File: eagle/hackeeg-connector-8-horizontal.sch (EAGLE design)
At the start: 21 parts

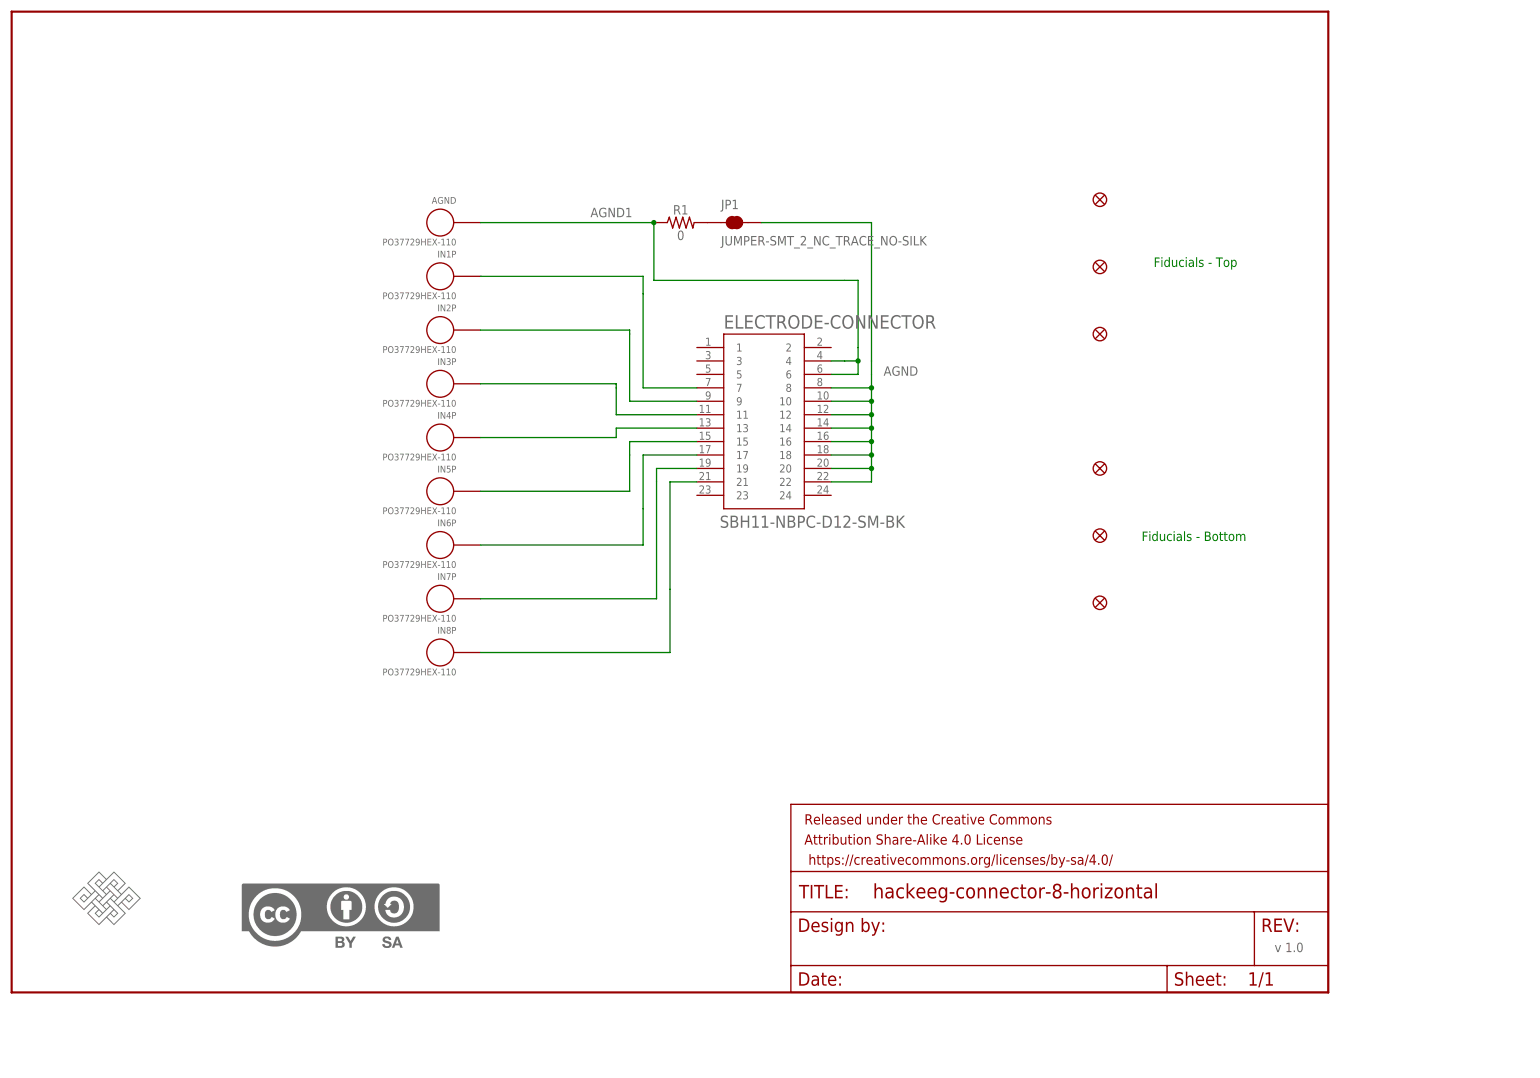
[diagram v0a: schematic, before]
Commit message: relicense to CERN OHL 1.2 - sch and brd
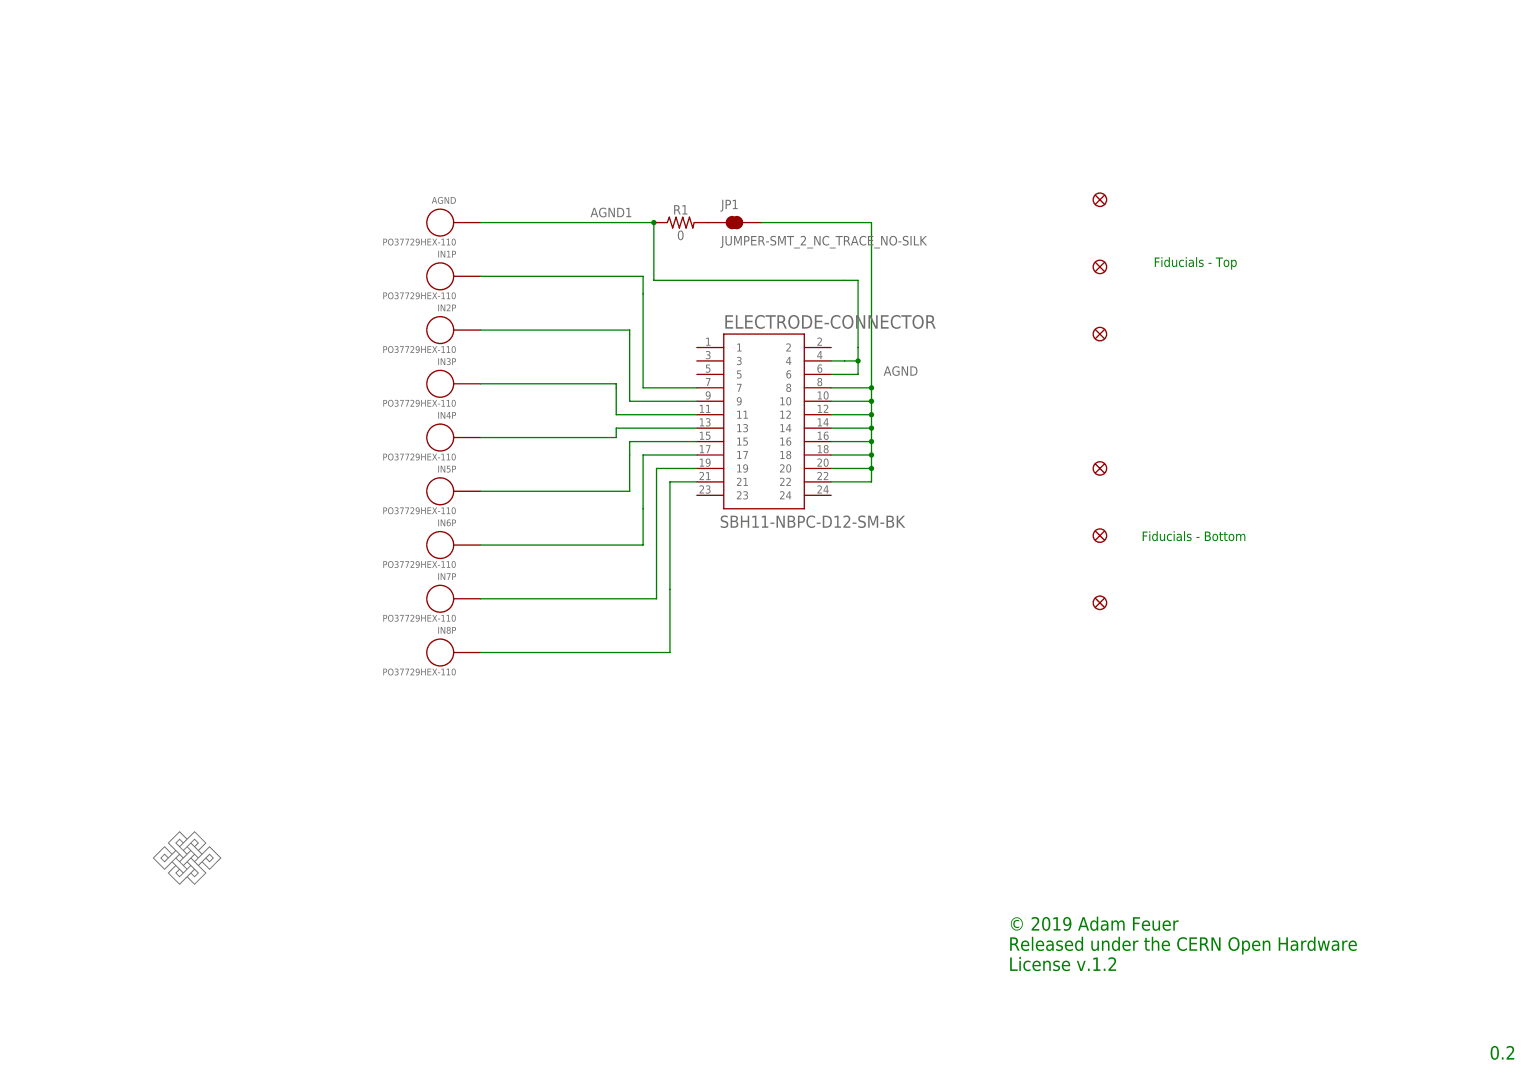
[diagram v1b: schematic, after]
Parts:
- removed FRAME1: FRAME-LETTER, SparkFun-Aesthetics:FRAME-LETTER
- removed U$13: CC-BY-SA, creative-commons:CC-BY-SA
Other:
- note added: "0.2"
- note added: "© 2019 Adam Feuer Released under the CERN Open Hardware License v.1.2"
- note removed: "v 1.0"
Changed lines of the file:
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@@
 <parts>
 <part name="IN1P" library="po-37729" deviceset="PO37729" device="HEX-110" value="PO37729HEX-110"/>
-<part name="FRAME1" library="SparkFun-Aesthetics" library_urn="urn:adsk.eagle:library:507" deviceset="FRAME-LETTER" device="" package3d_urn="urn:adsk.eagle:package:37121/1"/>
 <part name="ELECTRODE-CONNECTOR" library="SBH11-NBPC-D12-SM-BK" deviceset="SBH11-NBPC-D12-SM-BK" device=""/>
-<part name="U$13" library="creative-commons" deviceset="CC-BY-SA" device=""/>
 <part name="IN2P" library="po-37729" deviceset="PO37729" device="HEX-110" value="PO37729HEX-110"/>
 <part name="IN3P" library="po-37729" deviceset="PO37729" device="HEX-110" value="PO37729HEX-110"/>
@@
 <part name="R1" library="SparkFun-Resistors" library_urn="urn:adsk.eagle:library:532" deviceset="0OHM" device="-0603-1/10W-5%" package3d_urn="urn:adsk.eagle:package:39650/1" value="0"/>
 <part name="JP1" library="SparkFun-Jumpers" library_urn="urn:adsk.eagle:library:528" deviceset="JUMPER-SMT_2_NC_TRACE" device="_NO-SILK" package3d_urn="urn:adsk.eagle:package:39286/1"/>
+<part name="FRAME1" library="frames" library_urn="urn:adsk.eagle:library:229" deviceset="FRAME_A_L" device="" value="hackeeg-connector-8"/>
 </parts>
 <sheets>
@@
 <text x="365.76" y="182.88" size="1.778" layer="91">Fiducials - Top</text>
 <text x="363.474" y="131.064" size="1.778" layer="91">Fiducials - Bottom</text>
-<text x="388.62" y="53.34" size="1.778" layer="95">v 1.0</text>
+<text x="338.328" y="49.784" size="2.54" layer="91">© 2019 Adam Feuer
+Released under the CERN Open Hardware
+License v.1.2</text>
+<text x="429.26" y="33.02" size="2.54" layer="91">0.2</text>
 </plain>
 <instances>
@@
 <attribute name="VALUE" x="233.934" y="176.784" size="1.27" layer="95" rot="MR0"/>
 </instance>
-<instance part="FRAME1" gate="G$1" x="149.86" y="45.72" smashed="yes"/>
-<instance part="FRAME1" gate="V" x="297.18" y="45.72" smashed="yes">
-<attribute name="LAST_DATE_TIME" x="309.88" y="46.99" size="2.54" layer="94" font="vector"/>
-<attribute name="SHEET" x="383.54" y="46.99" size="2.54" layer="94" font="vector"/>
-<attribute name="DRAWING_NAME" x="312.674" y="63.5" size="2.7432" layer="94" font="vector"/>
-</instance>
 <instance part="ELECTRODE-CONNECTOR" gate="G$1" x="292.1" y="152.4" smashed="yes">
 <attribute name="NAME" x="284.48" y="171.20891875" size="2.54646875" layer="95"/>
 <attribute name="VALUE" x="283.718" y="133.5629" size="2.28846875" layer="96"/>
 </instance>
-<instance part="U$13" gate="G$1" x="193.04" y="53.34" smashed="yes"/>
 <instance part="IN2P" gate="G$1" x="238.506" y="170.942" smashed="yes" rot="MR0">
 <attribute name="NAME" x="233.934" y="174.498" size="1.27" layer="95" rot="MR0"/>
@@
 <attribute name="VALUE" x="233.934" y="105.664" size="1.27" layer="95" rot="MR0"/>
 </instance>
-<instance part="U$1" gate="G$1" x="167.64" y="63.5" smashed="yes"/>
+<instance part="U$1" gate="G$1" x="182.88" y="71.12" smashed="yes"/>
 <instance part="FD1" gate="G$1" x="355.6" y="170.18" smashed="yes"/>
 <instance part="FD2" gate="G$1" x="355.6" y="182.88" smashed="yes"/>
@@
 <attribute name="NAME" x="283.972" y="193.802" size="1.778" layer="95" font="vector"/>
 <attribute name="VALUE" x="283.972" y="188.722" size="1.778" layer="96" font="vector" align="top-left"/>
+</instance>
+<instance part="FRAME1" gate="G$1" x="162.56" y="25.4" smashed="yes"/>
+<instance part="FRAME1" gate="G$2" x="335.28" y="25.4" smashed="yes">
+<attribute name="LAST_DATE_TIME" x="347.98" y="26.67" size="2.54" layer="94"/>
+<attribute name="SHEET" x="421.64" y="26.67" size="2.54" layer="94"/>
+<attribute name="DRAWING_NAME" x="353.06" y="44.45" size="2.54" layer="94"/>
 </instance>
 </instances>
@@
 </drawing>
 <compatibility>
+<note version="6.3" minversion="6.2.2" severity="warning">
+Since Version 6.2.2 text objects can contain more than one line,
+which will not be processed correctly with this version.
+</note>
 <note version="8.2" severity="warning">
 Since Version 8.2, EAGLE supports online libraries. The ids
